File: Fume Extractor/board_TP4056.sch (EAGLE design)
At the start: 26 parts, among them IC1 BQ21040DBVR, IC2 DW01, J1 TYPE-C-31-M-17, T1 FS8205A, U2 MT3608

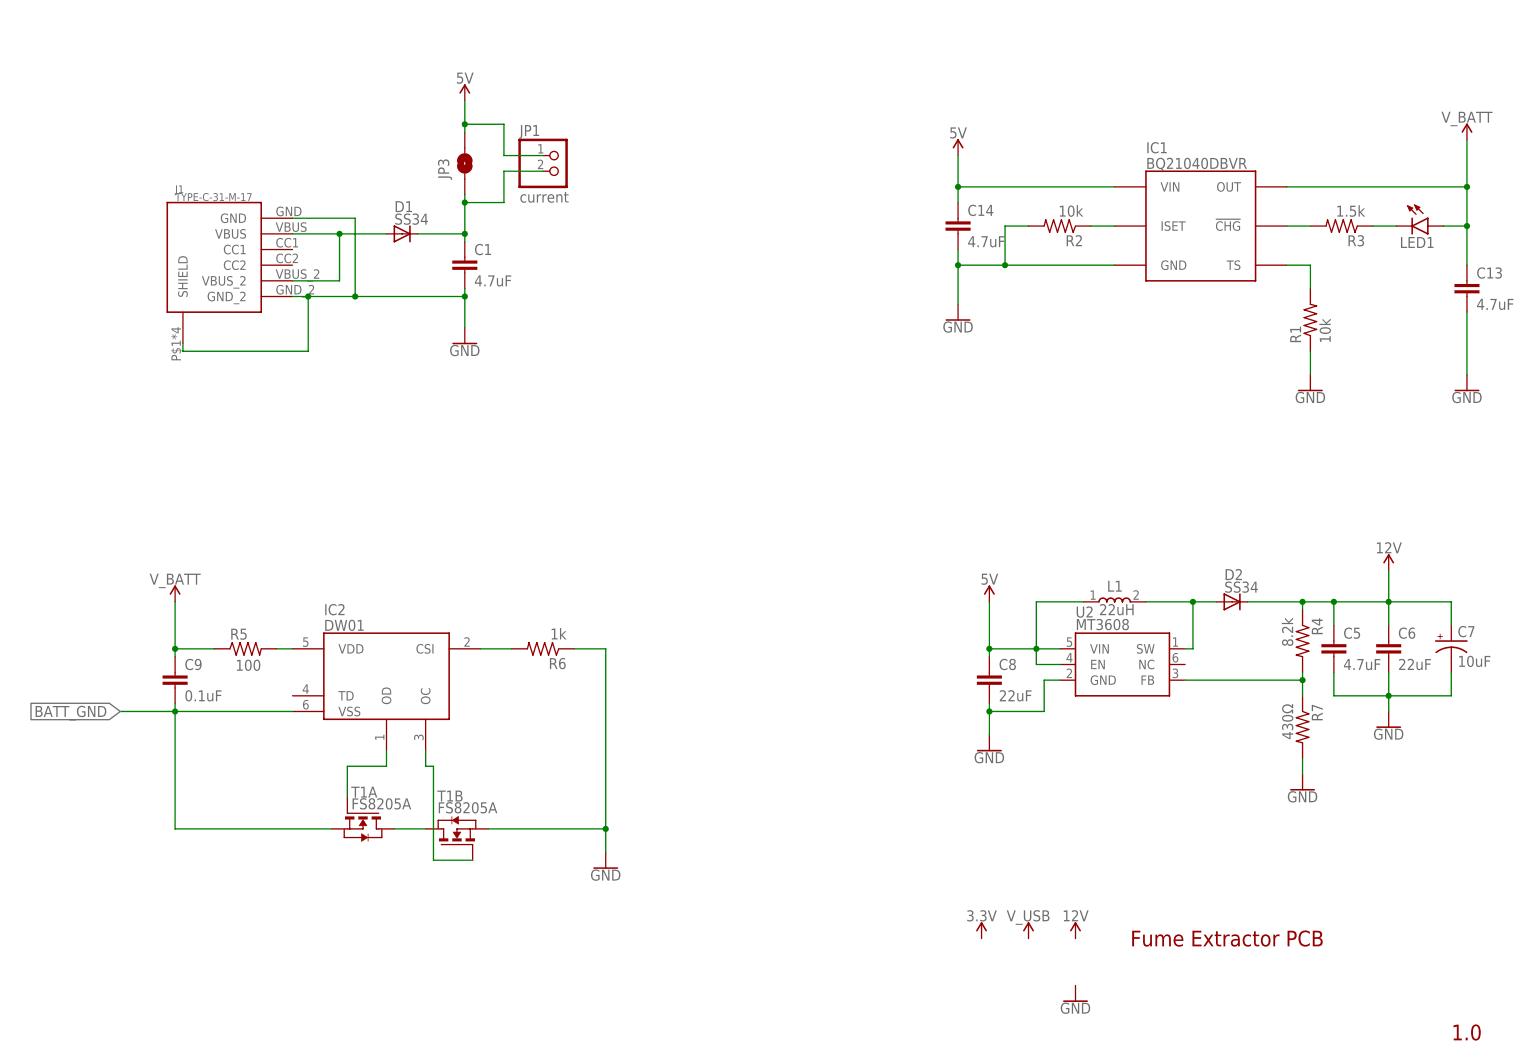
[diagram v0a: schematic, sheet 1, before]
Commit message: moving to BQ2104DBVR charging IC, backed up TP4056 circuit
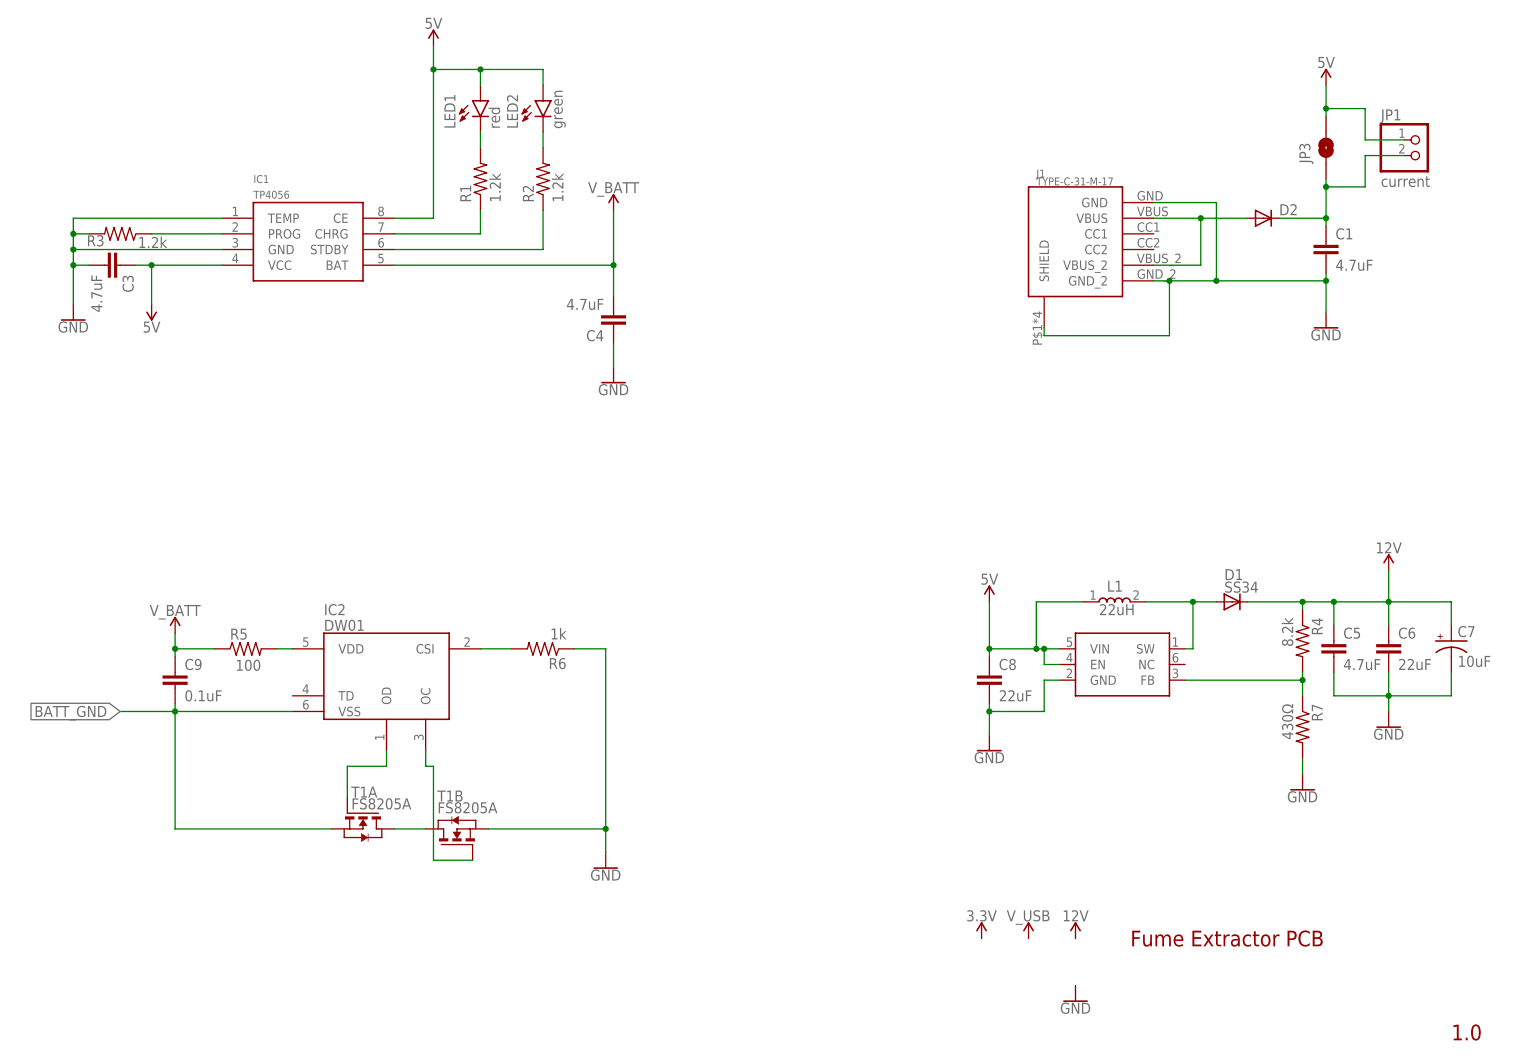
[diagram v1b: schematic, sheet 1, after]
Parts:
- removed C13, C14: 4.7uF, rcl:C-EUC0603
- added C3, C4: 4.7uF, rcl:C-EUC0805
- added LED2: green, led:LEDCHIP-LED0805
- D2: value SS34 -> (none); device diode:DIODE-DO214AC -> dp_devices:DIODE-SOD-123
- IC1: value BQ21040DBVR -> TP4056; device SamacSys_Parts:BQ21040DBVR -> TP4056:TP4056
- LED1: value (none) -> red; device led:LEDCHIP-LED0603 -> led:LEDCHIP-LED0805
- R1, R2: value 10k -> 1.2k; device rcl:R-US_R0402 -> rcl:R-US_R0805
- R3: value 1.5k -> 1.2k; device rcl:R-US_R0402 -> rcl:R-US_R0805
- renumbered U2 to U1
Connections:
- new net N$11: LED1.C, R1.2
- net 12V: now also D1.C; no longer D2.C
- net 5V: now also C3.1, IC1.CE, IC1.VCC, LED1.A, LED2.A; no longer C14.1, IC1.VIN
- net GND: now also C3.2, C4.1, IC1.TEMP, R3.2; no longer C13.2, C14.2, R1.1, R2.2
- net N$10: now also D1.A; no longer D2.A
- net N$13: now also D2.C; no longer D1.C
- net N$14: now also D2.A; no longer D1.A
- net N$2: now also IC1.CHRG, R1.1; no longer IC1.TS, R1.2
- net N$3: now also IC1.STDBY, R2.1; no longer IC1.!CHG, R3.2
- net N$8: now also IC1.PROG; no longer LED1.C
- net N$9: now also LED2.C, R2.2; no longer IC1.ISET, R2.1
- net V_BATT: now also C4.2, IC1.BAT; no longer C13.1, IC1.OUT, LED1.A
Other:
- moved on the sheet: C1, D1, J1, JP1, JP3, LED1, R1, R2, R3
